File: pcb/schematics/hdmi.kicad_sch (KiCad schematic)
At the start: 0 parts

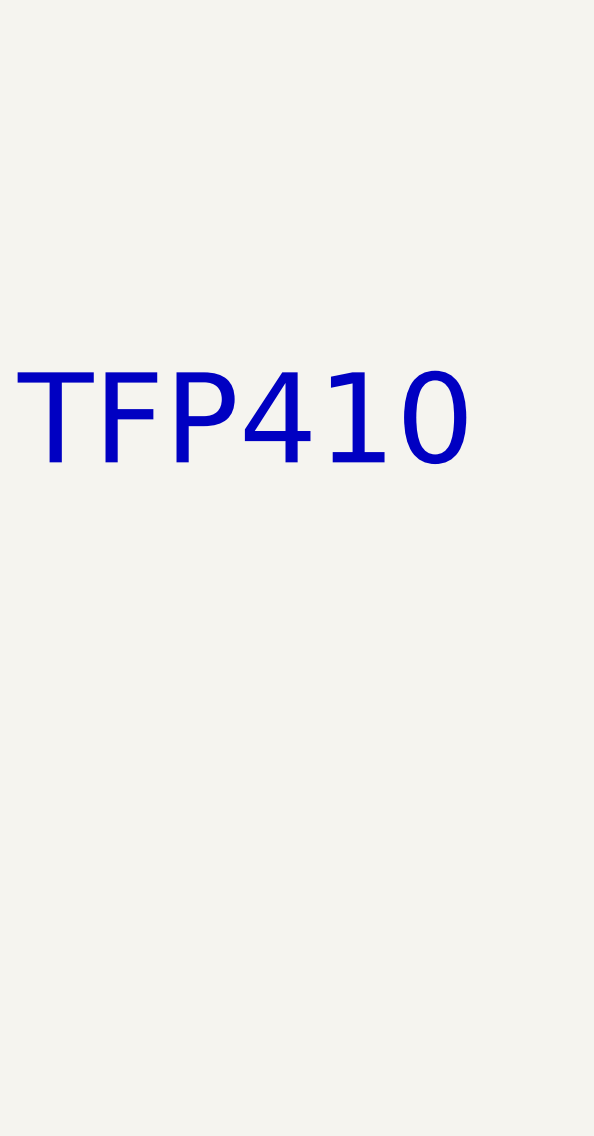
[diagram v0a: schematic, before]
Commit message: add architecture diagramé
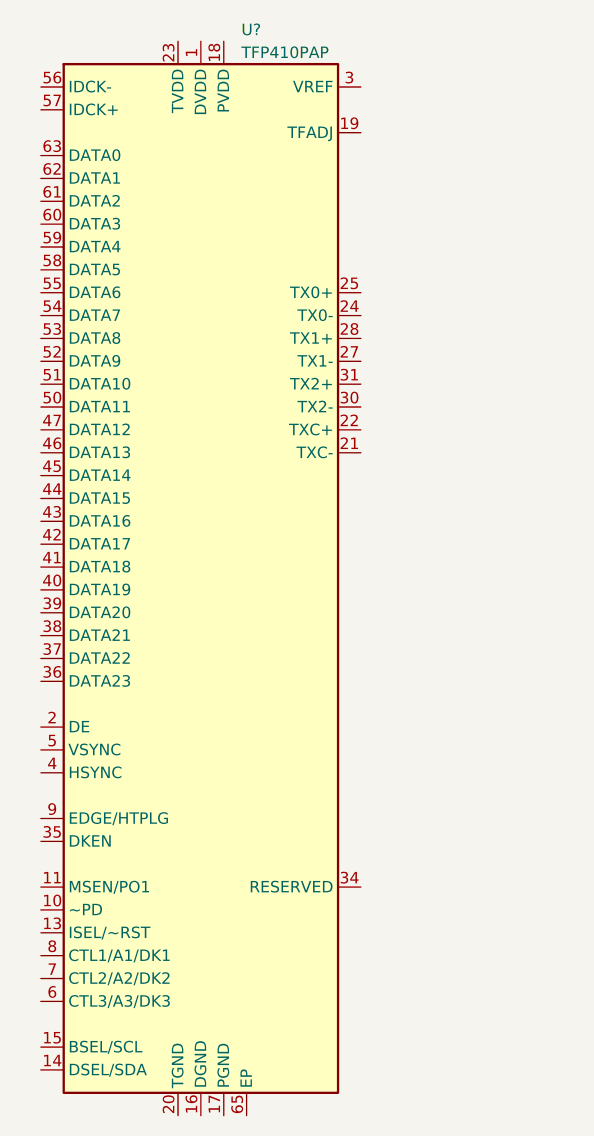
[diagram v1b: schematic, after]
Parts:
- added U?: TFP410PAP, Package_QFP:HTQFP-64-1EP_10x10mm_P0.5mm_EP8x8mm_Mask4.4x4.4mm_ThermalVias, symbol Video:TFP410PAP
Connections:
- new net: U?.1 (DVDD), U?.12 (DVDD), U?.33 (DVDD)
- new net: U?.16 (DGND), U?.48 (DGND), U?.64 (DGND)
- new net: U?.20 (TGND), U?.26 (TGND), U?.32 (TGND)
- new net: U?.23 (TVDD), U?.29 (TVDD)
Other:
- note removed: "TFP410"
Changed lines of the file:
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@@
 (kicad_sch (version 20220126) (generator eeschema)
   (paper "A4")
-  (text "TFP410" (at 119.38 91.44 0)
-    (effects (font (size 10 10)) (justify left bottom))
+  (symbol (lib_id "Video:TFP410PAP") (at 139.7 101.6 0) (unit 1)
+    (in_bom yes) (on_board yes) (fields_autoplaced)
+    (property "Reference" "U?" (id 0) (at 144.1959 41.91 0)
+      (effects (font (size 1.27 1.27)) (justify left))
+    )
+    (property "Value" "TFP410PAP" (id 1) (at 144.1959 44.45 0)
+      (effects (font (size 1.27 1.27)) (justify left))
+    )
+    (property "Footprint" "Package_QFP:HTQFP-64-1EP_10x10mm_P0.5mm_EP8x8mm_Mask4.4x4.4mm_ThermalVias" (id 2) (at 140.97 162.56 0)
+      (effects (font (size 1.27 1.27)) hide)
+    )
+    (property "Datasheet" "http://www.ti.com/lit/ds/symlink/tfp410.pdf" (id 3) (at 140.97 161.29 0)
+      (effects (font (size 1.27 1.27)) hide)
+    )
+    (pin "1")
+    (pin "10")
+    (pin "11")
+    (pin "12")
+    (pin "13")
+    (pin "14")
+    (pin "15")
+    (pin "16")
+    (pin "17")
+    (pin "18")
+    (pin "19")
+    (pin "2")
+    (pin "20")
+    (pin "21")
+    (pin "22")
+    (pin "23")
+    (pin "24")
+    (pin "25")
+    (pin "26")
+    (pin "27")
+    (pin "28")
+    (pin "29")
+    (pin "3")
+    (pin "30")
+    (pin "31")
+    (pin "32")
+    (pin "33")
+    (pin "34")
+    (pin "35")
+    (pin "36")
+    (pin "37")
+    (pin "38")
+    (pin "39")
+    (pin "4")
+    (pin "40")
+    (pin "41")
+    (pin "42")
+    (pin "43")
+    (pin "44")
+    (pin "45")
+    (pin "46")
+    (pin "47")
+    (pin "48")
+    (pin "49")
+    (pin "5")
+    (pin "50")
+    (pin "51")
+    (pin "52")
+    (pin "53")
+    (pin "54")
+    (pin "55")
+    (pin "56")
+    (pin "57")
+    (pin "58")
+    (pin "59")
+    (pin "6")
+    (pin "60")
+    (pin "61")
+    (pin "62")
+    (pin "63")
+    (pin "64")
+    (pin "65")
+    (pin "7")
+    (pin "8")
+    (pin "9")
   )
 )

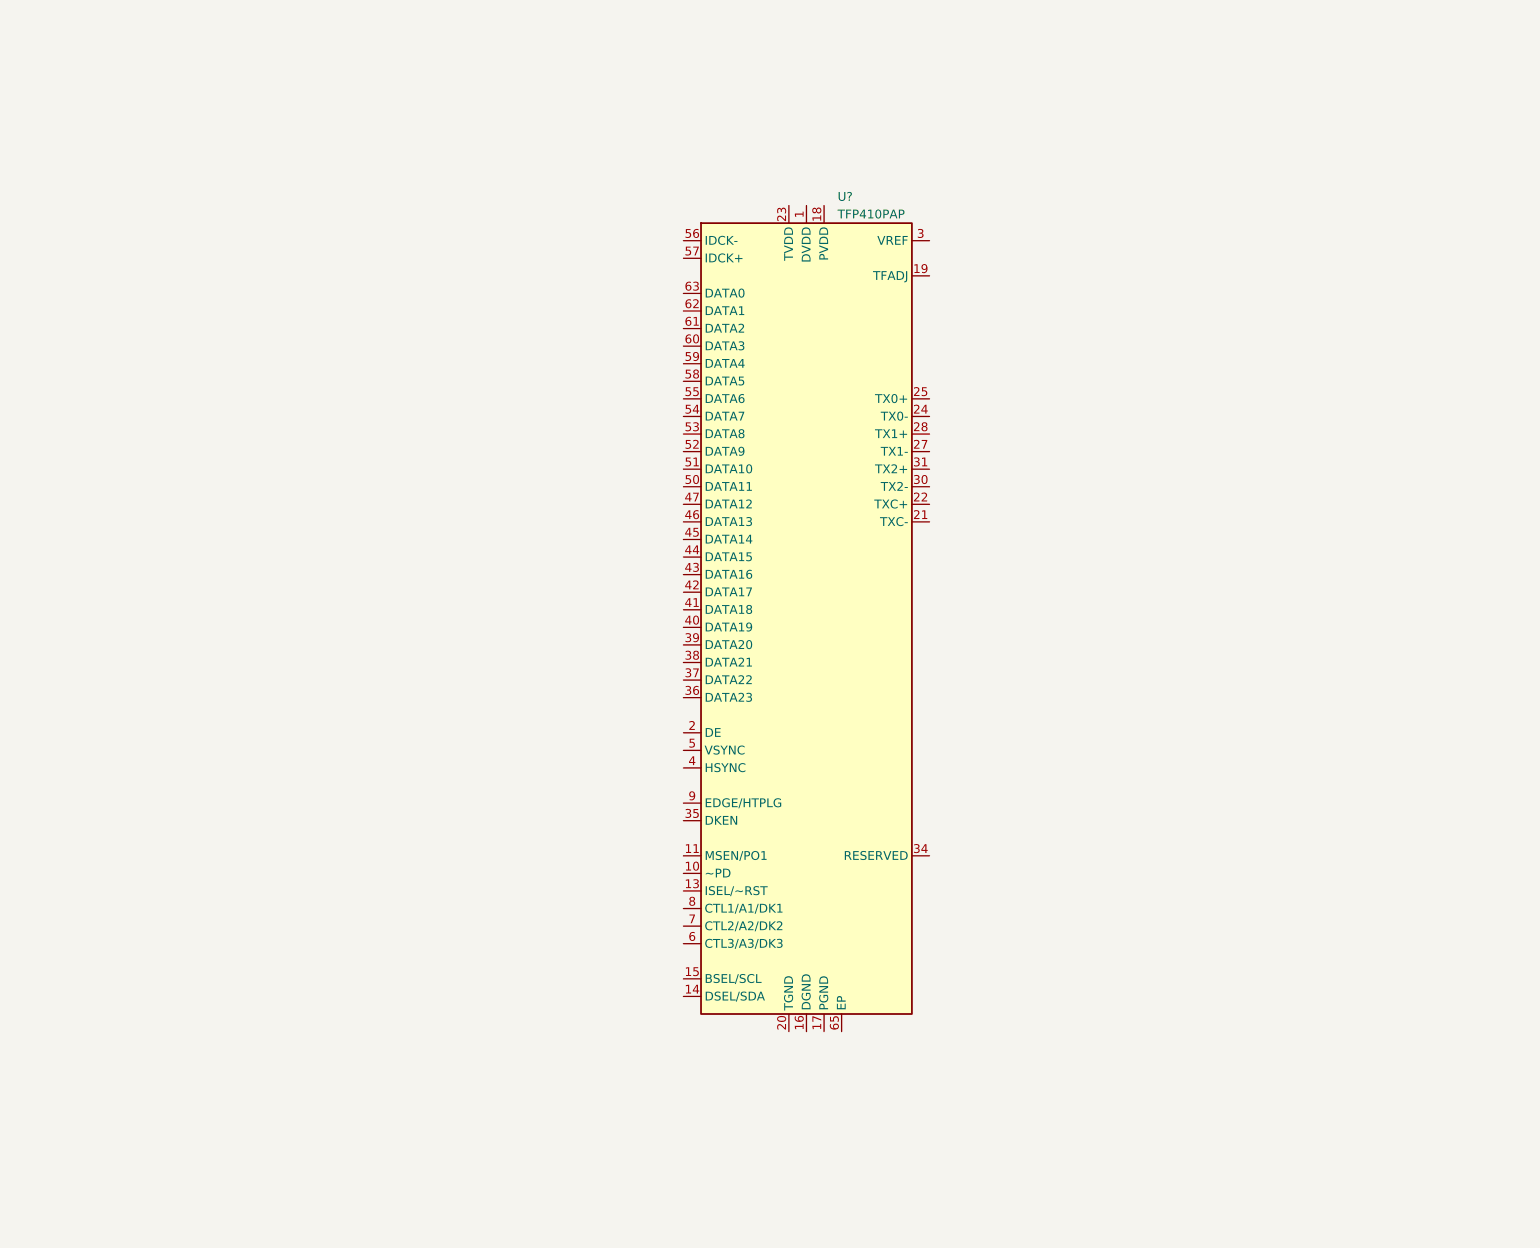
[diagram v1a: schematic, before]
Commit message: start adding decoupling caps for the hdmi frontend
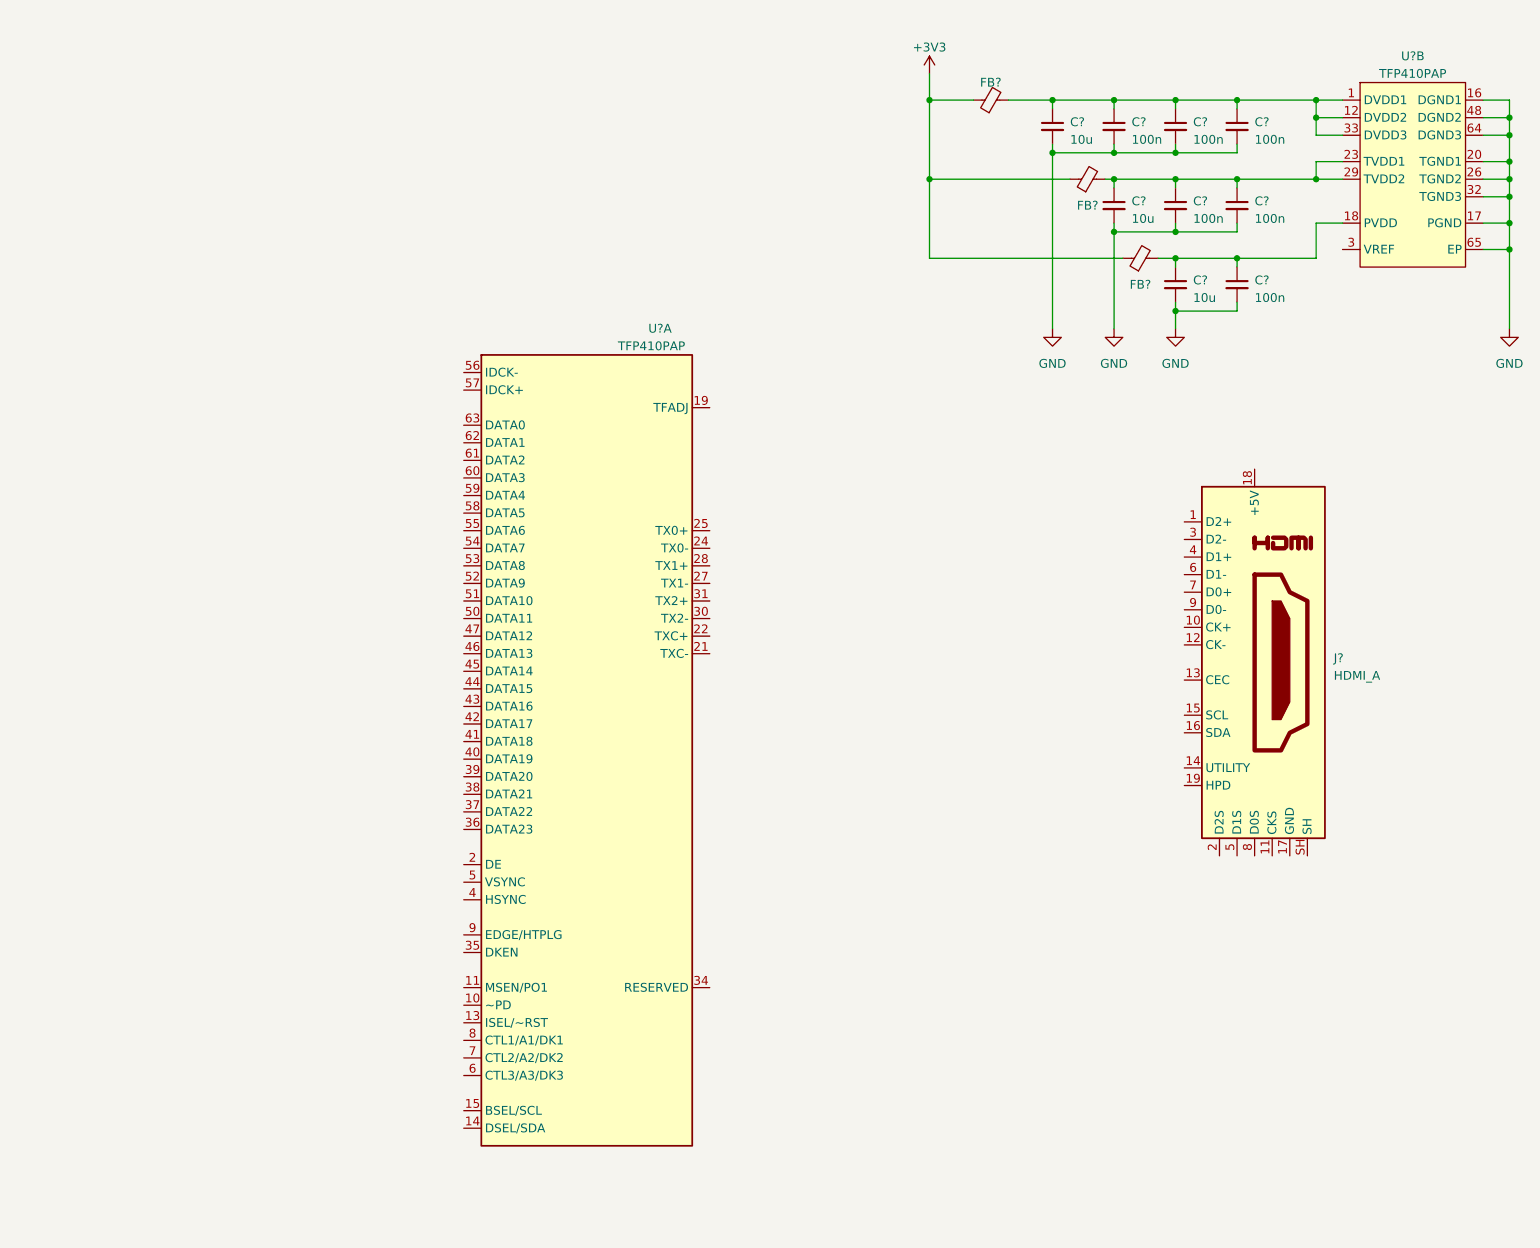
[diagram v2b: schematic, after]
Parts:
- added C? (x3): 10u, symbol Device:C_Small
- added C? (x6): 100n, symbol Device:C_Small
- added FB? (x3): FerriteBead_Small, symbol Device:FerriteBead_Small
- added J?: HDMI_A, symbol Connector:HDMI_A
- added U?: TFP410PAP, Package_QFP:HTQFP-64-1EP_10x10mm_P0.5mm_EP8x8mm_Mask4.4x4.4mm_ThermalVias, symbol Video:TFP410PAP
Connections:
- new net: C?.1, C?.1, FB?.2, U?.18 (PVDD)
- new net: C?.1, C?.1, C?.1, C?.1, FB?.2, U?.1 (DVDD1), U?.12 (DVDD2), U?.33 (DVDD3)
- new net: C?.1, C?.1, C?.1, FB?.2, U?.23 (TVDD1), U?.29 (TVDD2)
- new net +3V3: FB?.1, FB?.1, FB?.1
- new net GND: C?.2, C?.2, C?.2, C?.2, C?.2, C?.2, C?.2, C?.2, C?.2, U?.16 (DGND1), U?.17 (PGND), U?.20 (TGND1), U?.26 (TGND2), U?.32 (TGND3), U?.48 (DGND2), U?.64 (DGND3), U?.65 (EP)

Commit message: start adding schematic for the hdmi frontend
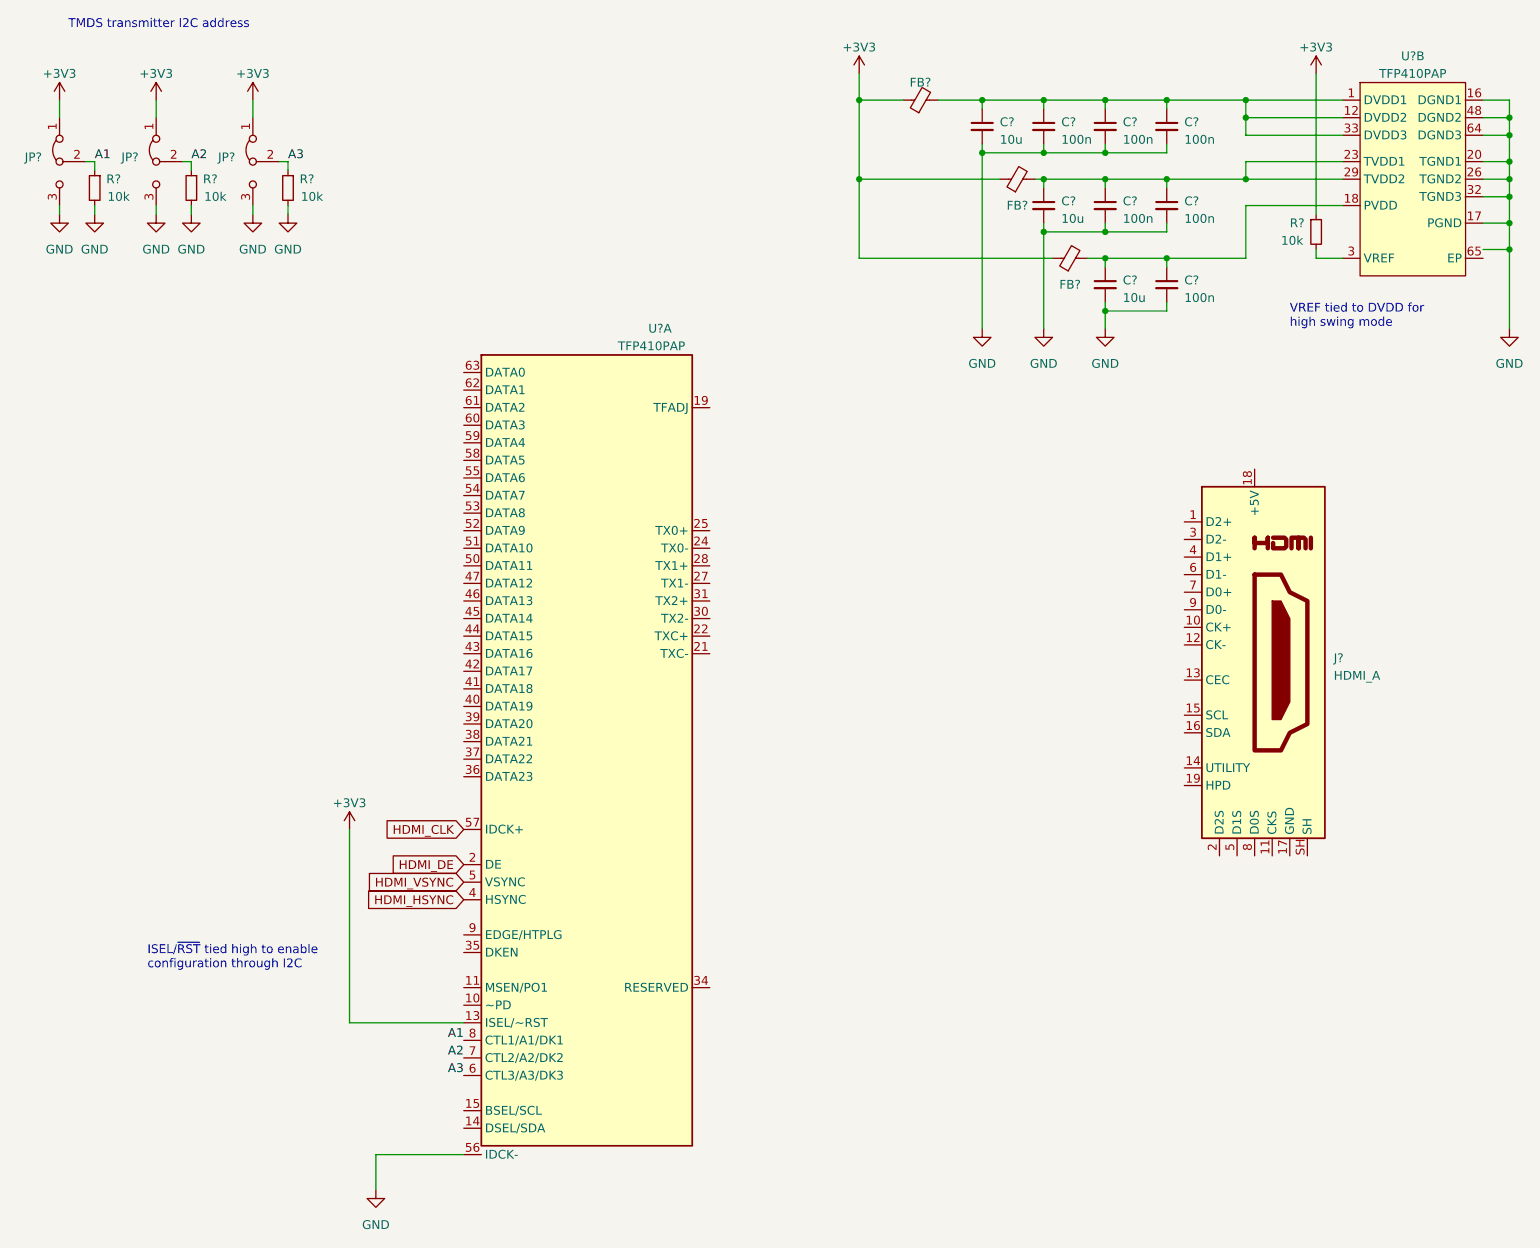
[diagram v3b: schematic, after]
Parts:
- added JP? (x3): Jumper_3_Bridged12, symbol Jumper:Jumper_3_Bridged12
- added R? (x4): 10k, symbol Device:R_Small
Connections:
- net +3V3: now also U?.13 (ISEL/~RST), JP?.1 (A), JP?.1 (A), JP?.1 (A), R?.1
- net GND: now also U?.56 (IDCK-), JP?.3 (B), JP?.3 (B), JP?.3 (B), R?.2, R?.2, R?.2; no longer U?.65 (EP)
- net HDMI_DE: now reaches U?.2 (DE)
- net HDMI_HSYNC: now reaches U?.4 (HSYNC)
- net HDMI_VSYNC: now reaches U?.5 (VSYNC)
- net HDMI_CLK: now reaches U?.57 (IDCK+)
- net A3: now reaches U?.6 (CTL3/A3/DK3)
- net A3: now also JP?.2 (C), R?.1
- net A2: now reaches U?.7 (CTL2/A2/DK2)
- net A2: now also JP?.2 (C), R?.1
- net A1: now reaches U?.8 (CTL1/A1/DK1)
- net A1: now also JP?.2 (C), R?.1
- net at U?.3 (VREF): now also R?.2
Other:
- note added: "ISEL/~{RST} tied high to enable configuration through I2C"
- note added: "TMDS transmitter I2C address"
- note added: "VREF tied to DVDD for high swing mode"
- moved on the sheet: C?, FB?, U?A, U?B
